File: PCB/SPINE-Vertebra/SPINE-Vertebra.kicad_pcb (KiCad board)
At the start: 2 copper layers, 49 x 49 mm, 75 parts, among them J2 Conn_01x06, J4 Conn_01x06, Q1 NTMFS5C628NLT1G, Q2 NTMFS5C628NLT1G, Q3 NTMFS5C628NLT1G, Q4 NTMFS5C628NLT1G, Q7 VISHAY SI2309CDS-T1-GE3, Q8 Q_NMOS_GSD, U1 ACS724xLCTR-50AB, U2 LM74800QDRRRQ1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

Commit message: Finish Vertebra
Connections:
- C7 pad 2: +5V -> +3.3V
- U3 pad 8: +5V -> +3.3V
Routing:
- net +5V: track 72.7 -> 39.3 mm, vias 2 -> 1
- net +3.3V: track 19.6 -> 28.5 mm

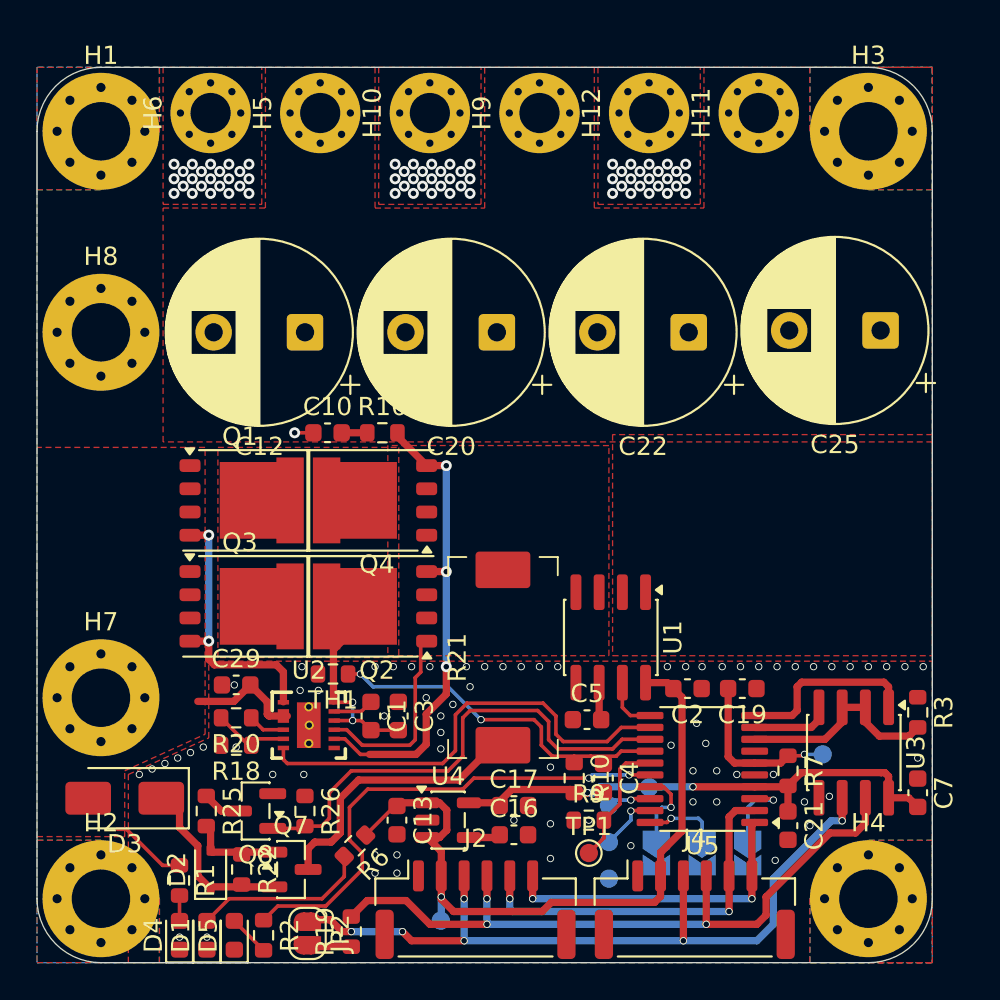
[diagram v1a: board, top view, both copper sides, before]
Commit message: Vertebra fix
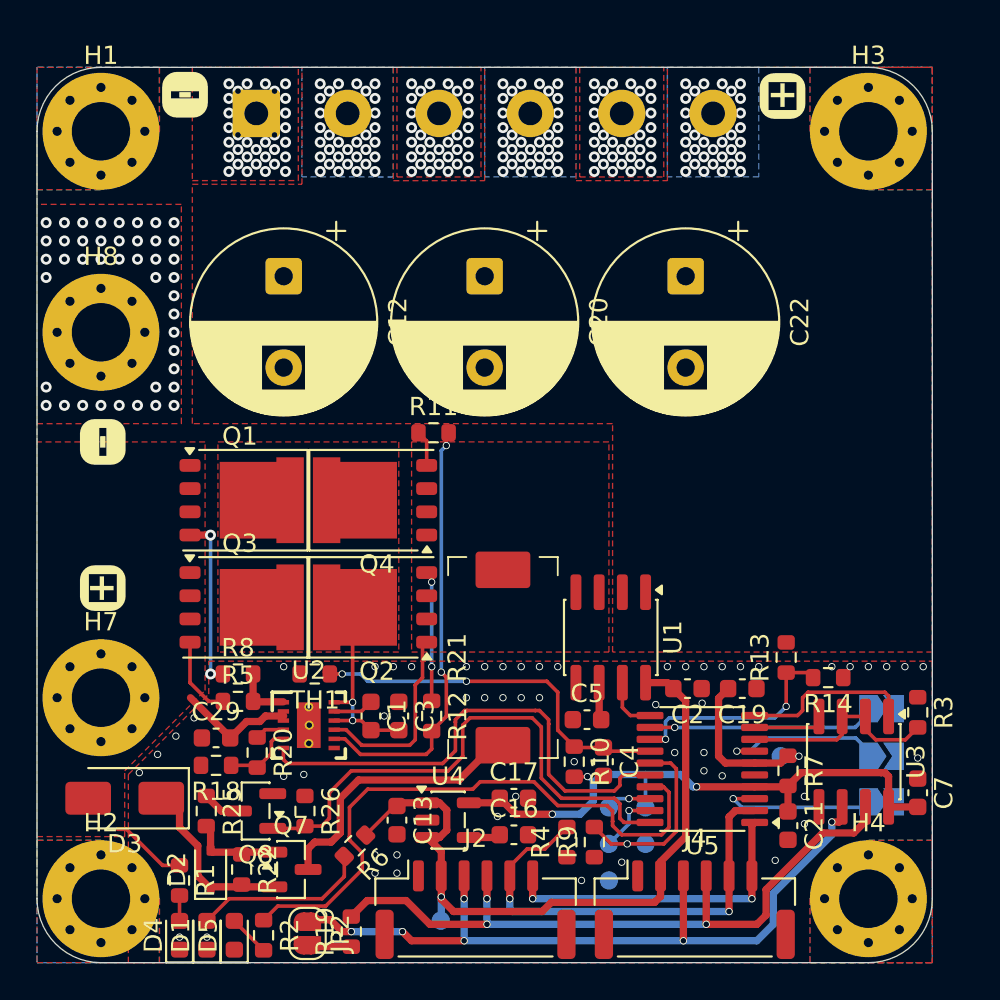
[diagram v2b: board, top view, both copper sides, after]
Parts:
- removed C10: 100nF, Capacitor_SMD:C_0603_1608Metric
- removed C25: 100uF, Capacitor_THT:CP_Radial_D10.0mm_P5.00mm
- removed H10, H11, H12, H5, H6, H9: MountingHole_Pad, MountingHole:MountingHole_2.2mm_M2_Pad_Via
- removed R16: 1K, Resistor_SMD:R_0603_1608Metric
- added J6: POWER, TerminalBlock_MetzConnect:TerminalBlock_MetzConnect_Type094_RT03506HBLU_1x06_P5.00mm_Horizontal, F.Cu at (87.5, 78.0)
- added R11: 1K, Resistor_SMD:R_0603_1608Metric, F.Cu at (97.2, 95.5)
- added R12: 1K, Resistor_SMD:R_0603_1608Metric, F.Cu at (97.1, 111.0)
- added R13: 10K, Resistor_SMD:R_0603_1608Metric, F.Cu at (116.5, 107.8)
- added R14: 10K, Resistor_SMD:R_0603_1608Metric, F.Cu at (118.8, 108.9)
- added R4: 10K, Resistor_SMD:R_0603_1608Metric, F.Cu at (104.5, 117.9)
- added R5: 1K, Resistor_SMD:R_0603_1608Metric, F.Cu at (86.5, 110.2)
- added R8: 1K, Resistor_SMD:R_0603_1608Metric, F.Cu at (86.5, 108.7)
- D1, D4, D5: value LED_Small -> LED
- TP1: moved to B.Cu
- moved G*** 30.4 mm to (117.0, 100.0), turned to -90 degrees
- moved JP1 12.6 mm to (121.7, 115.7), turned to 0 degrees
- moved JP3 11.2 mm to (121.7, 113.2), turned to 0 degrees
- moved JP4 10.8 mm to (121.7, 110.6), turned to 0 degrees
- moved C12 3.28 mm to (89.0, 86.9), turned to -90 degrees
- moved TP1 3.14 mm to (108.8, 118.0)
- moved C20 3.14 mm to (100.0, 86.9), turned to -90 degrees
- moved C29 3.10 mm to (85.3, 112.2)
- moved C22 3.07 mm to (111.0, 86.9), turned to -90 degrees
- moved TP2 2.30 mm to (116.2, 113.2)
- moved R20 2.22 mm to (87.5, 113.0), turned to -90 degrees
- moved R18 1.56 mm to (85.3, 113.7)
- moved R9 1.24 mm to (106.0, 117.9), turned to 90 degrees
- moved TP3 1.12 mm to (108.8, 116.0)
- moved TH1 1.00 mm to (90.7, 108.7)
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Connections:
- J2 pad 5: FAULT -> ENABLE
- J2 pad 6: ENABLE -> FAULT
- J4 pad 5: FAULT -> ENABLE
- J4 pad 6: ENABLE -> FAULT
- Q1 pad 4: DGATE -> Net-(Q1-G)
- Q2 pad 4: HGATE -> Net-(Q2-G)
- Q3 pad 4: DGATE -> Net-(Q3-G)
- Q4 pad 4: HGATE -> Net-(Q4-G)
- U5 pad 1: ENABLE -> FAULT
- U5 pad 12: ORING_EN -> ID1
- U5 pad 13: PRE-CHARGE_EN -> VOLTAGE_SENSE
- U5 pad 16: LED_1 -> ORING_EN
- U5 pad 17: ID3 -> LED_1
- U5 pad 2: FAULT -> ENABLE
- U5 pad 20: ID2 -> PRE-CHARGE_EN
- U5 pad 3: ID1 -> ID3
- U5 pad 7: unconnected-(U5-PA0-Pad7) -> ID2
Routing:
- net VOLTAGE_SENSE: track 0.00 -> 12.2 mm, vias 0 -> 2
- net DGATE: track 14.9 -> 3.17 mm, vias 2 -> 0
- net Net-(Q1-G): track 0.00 -> 9.40 mm, vias 0 -> 2
- net ID1: track 4.40 -> 13.0 mm
- net ENABLE: track 18.1 -> 25.7 mm
- net Net-(Q2-G): track 0.00 -> 7.14 mm, vias 0 -> 2
- net LED_1: track 27.4 -> 33.2 mm, vias 2 -> 0
- net ID2: track 4.00 -> 8.87 mm
- net +3.3V: track 28.5 -> 33.3 mm, vias 2 -> 3
- net Net-(Q3-G): track 0.00 -> 4.44 mm
- net ID3: track 4.43 -> 8.85 mm
- net BOOT: track 7.09 -> 11.1 mm, vias 0 -> 1
- net FAULT: track 21.2 -> 18.1 mm
- net PRE-CHARGE_EN: track 27.0 -> 29.5 mm
- net ORING_EN: track 25.1 -> 27.2 mm
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- added copper zone on B.Cu, net VDC
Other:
- board text added: "+"
- board text added: "-"
- board text added: "BOOT"

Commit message: update
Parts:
- removed D5: LED, LED_SMD:LED_0603_1608Metric
- removed R2: 1K, Resistor_SMD:R_0603_1608Metric
- added D6: WS2812B-2020, LED_SMD:LED_WS2812B-2020_PLCC4_2.0x2.0mm, F.Cu at (87.2, 122.8)
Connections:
- net SENSE_Out renamed CURRENT_SENSE
- U5 pad 12: ID1 -> VOLTAGE_SENSE
- U5 pad 13: VOLTAGE_SENSE -> ID1
- U5 pad 17: LED_1 -> unconnected-(U5-PA10/PA12-Pad17)
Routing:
- net LED_1: track 33.2 -> 0.00 mm
- net BOOT: track 11.1 -> 36.4 mm
- net +5V: track 39.5 -> 53.5 mm, vias 1 -> 2
- net Net-(D5-A): track 2.28 -> 0.00 mm
- net VOLTAGE_SENSE: track 12.2 -> 11.4 mm
- net GND: vias 194 -> 196

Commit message: update
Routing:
- net +3.3V: track 33.3 -> 34.7 mm
- net +5V: track 53.5 -> 52.4 mm
- net BOOT: track 36.4 -> 35.7 mm
- net PRE-CHARGE_EN: track 29.5 -> 28.7 mm
- net USART2_DE: track 11.3 -> 10.7 mm
- net RS485_B: track 39.4 -> 38.9 mm
